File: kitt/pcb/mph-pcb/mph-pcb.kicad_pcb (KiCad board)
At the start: 4 copper layers, 280 x 125 mm, 6 parts

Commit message: prototype layout
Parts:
- added REF**: DF3GD, KITT-Footpads:DF3GD_Light_Bar, F.Cu at (123.8, 80.3)
- added REF**: LED, KITT-Footpads:Flangeless_LED, F.Cu at (122.5, 107.0)
- added REF**: LED, KITT-Footpads:Flangeless_LED, F.Cu at (117.4, 107.0)
- added REF**: LED, KITT-Footpads:Flangeless_LED, F.Cu at (112.3, 107.0)
- added REF**: LED, KITT-Footpads:Flangeless_LED, F.Cu at (107.2, 107.0)
- added REF**: LED, KITT-Footpads:Flangeless_LED, F.Cu at (102.2, 107.0)
- added REF**: LED, KITT-Footpads:Flangeless_LED, F.Cu at (97.1, 107.0)
- added REF**: LED, KITT-Footpads:Flangeless_LED, F.Cu at (92.0, 107.0)
- added REF**: LED, KITT-Footpads:Flangeless_LED, F.Cu at (86.9, 107.0)
- added REF**: LED, KITT-Footpads:Flangeless_LED, F.Cu at (81.8, 107.0)
- added REF**: LED, KITT-Footpads:Flangeless_LED, F.Cu at (76.8, 107.0)
- added REF**: DF3GD, KITT-Footpads:DF3GD_Light_Bar, F.Cu at (103.4, 80.3)
- added REF**: LED, KITT-Footpads:Flangeless_LED, F.Cu at (71.7, 107.0)
- added REF**: LED, KITT-Footpads:Flangeless_LED, F.Cu at (66.6, 107.0)
- added REF**: LED, KITT-Footpads:Flangeless_LED, F.Cu at (61.5, 107.0)
- added REF**: LED, KITT-Footpads:Flangeless_LED, F.Cu at (56.4, 107.0)
- added REF**: LED, KITT-Footpads:Flangeless_LED, F.Cu at (51.4, 107.0)
- added REF**: LED, KITT-Footpads:Flangeless_LED, F.Cu at (48.8, 99.3)
- added REF**: LED, KITT-Footpads:Flangeless_LED, F.Cu at (53.9, 99.3)
- added REF**: LED, KITT-Footpads:Flangeless_LED, F.Cu at (59.0, 99.3)
- added REF**: LED, KITT-Footpads:Flangeless_LED, F.Cu at (117.4, 67.6)
- added REF**: LED, KITT-Footpads:Flangeless_LED, F.Cu at (122.5, 67.6)
- added REF**: DF3GD, KITT-Footpads:DF3GD_Light_Bar, F.Cu at (111.0, 91.7)
- added REF**: LED, KITT-Footpads:Flangeless_LED, F.Cu at (127.6, 67.6)
- added REF**: LED, KITT-Footpads:Flangeless_LED, F.Cu at (165.7, 99.3)
- added REF**: LED, KITT-Footpads:Flangeless_LED, F.Cu at (160.6, 99.3)
- added REF**: LED, KITT-Footpads:Flangeless_LED, F.Cu at (155.5, 99.3)
- added REF**: KB2855SGD, KITT-Footpads:KB2855SGD_Light_Square, F.Cu at (244.4, 84.1)
- added REF**: KB2855SGD, KITT-Footpads:KB2855SGD_Light_Square, F.Cu at (234.2, 84.1)
- added REF**: KB2855SGD, KITT-Footpads:KB2855SGD_Light_Square, F.Cu at (224.1, 84.1)
- added REF**: LDS-A816RI, KITT-Footpads:LDS-A816RI, F.Cu at (196.1, 70.1)
- added REF**: LED, KITT-Footpads:Flangeless_LED, F.Cu at (252.0, 60.0)
- added REF**: LED, KITT-Footpads:Flangeless_LED, F.Cu at (246.9, 60.0)
- added REF**: DF3GD, KITT-Footpads:DF3GD_Light_Bar, F.Cu at (90.7, 91.7)
- added REF**: LED, KITT-Footpads:Flangeless_LED, F.Cu at (241.9, 60.0)
- added REF**: LED, KITT-Footpads:Flangeless_LED, F.Cu at (236.8, 60.0)
- added REF**: LED, KITT-Footpads:Flangeless_LED, F.Cu at (231.7, 60.0)
- added REF**: LED, KITT-Footpads:Flangeless_LED, F.Cu at (226.6, 60.0)
- added REF**: LED, KITT-Footpads:Flangeless_LED, F.Cu at (221.5, 60.0)
- added REF**: LED, KITT-Footpads:Flangeless_LED, F.Cu at (216.5, 60.0)
- added REF**: LED, KITT-Footpads:Flangeless_LED, F.Cu at (211.4, 60.0)
- added REF**: LED, KITT-Footpads:Flangeless_LED, F.Cu at (206.3, 60.0)
- added REF**: LED, KITT-Footpads:Flangeless_LED, F.Cu at (201.2, 60.0)
- added REF**: LED, KITT-Footpads:Flangeless_LED, F.Cu at (196.1, 60.0)
- added REF**: LDS-A816RI, KITT-Footpads:LDS-A816RI, F.Cu at (112.3, 117.1)
- added REF**: LED, KITT-Footpads:Flangeless_LED, F.Cu at (191.1, 60.0)
- added REF**: LED, KITT-Footpads:Flangeless_LED, F.Cu at (186.0, 60.0)
- added REF**: LED, KITT-Footpads:Flangeless_LED, F.Cu at (180.9, 60.0)
- added REF**: LED, KITT-Footpads:Flangeless_LED, F.Cu at (175.8, 60.0)
- added REF**: LED, KITT-Footpads:Flangeless_LED, F.Cu at (170.7, 60.0)
- added REF**: LED, KITT-Footpads:Flangeless_LED, F.Cu at (165.7, 60.0)
- added REF**: LDS-A816RI, KITT-Footpads:LDS-A816RI, F.Cu at (175.8, 70.1)
- added REF**: LDS-A816RI, KITT-Footpads:LDS-A816RI, F.Cu at (155.5, 70.1)
- added REF**: LED, KITT-Footpads:Flangeless_LED, F.Cu at (165.7, 52.3)
- added REF**: LED, KITT-Footpads:Flangeless_LED, F.Cu at (160.6, 52.3)
- added REF**: LDS-A816RI, KITT-Footpads:LDS-A816RI, F.Cu at (92.0, 117.1)
- added REF**: LED, KITT-Footpads:Flangeless_LED, F.Cu at (155.5, 52.3)
- added REF**: LED, KITT-Footpads:Flangeless_LED, F.Cu at (160.6, 59.9)
- added REF**: LED, KITT-Footpads:Flangeless_LED, F.Cu at (155.5, 60.0)
- added REF**: LDS-A816RI, KITT-Footpads:LDS-A816RI, F.Cu at (71.7, 117.1)
- added REF**: LDS-A816RI, KITT-Footpads:LDS-A816RI, F.Cu at (51.4, 117.1)
- added REF**: LED, KITT-Footpads:Flangeless_LED, F.Cu at (127.6, 107.0)
- renumbered UL to MH1, UR to MH2, LR to MH3, LR to MH4
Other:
- board text added: "0"
- board text added: "100"
- board text added: "200"

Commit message: add pegboard holes
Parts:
- added PEG1: MountingHole_6.4mm_M6, MountingHole:MountingHole_6.4mm_M6, F.Cu at (58.1, 77.5)
- added PEG2: MountingHole_6.4mm_M6, MountingHole:MountingHole_6.4mm_M6, F.Cu at (286.7, 52.0)
- added PEG3: MountingHole_6.4mm_M6, MountingHole:MountingHole_6.4mm_M6, F.Cu at (58.1, 153.7)
- added PEG4: MountingHole_6.4mm_M6, MountingHole:MountingHole_6.4mm_M6, F.Cu at (261.3, 153.7)
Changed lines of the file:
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@@
     (tracks 0)
     (zones 0)
-    (modules 68)
+    (modules 72)
     (nets 1)
   )
@@
     (uvia_drill 0.1)
   )
+  (module MountingHole:MountingHole_6.4mm_M6 (layer F.Cu)
+    (at 286.7 52.05)
+    (descr "Mounting Hole 6.4mm, no annular, M6")
+    (tags "mounting hole 6.4mm no annular m6")
+    (attr virtual)
+    (fp_text reference PEG2 (at 0 -7.4) (layer F.SilkS)
+      (effects (font (size 1 1) (thickness 0.15)))
+    )
+    (fp_text value MountingHole_6.4mm_M6 (at 0 7.4) (layer F.Fab)
+      (effects (font (size 1 1) (thickness 0.15)))
+    )
+    (fp_circle (center 0 0) (end 6.65 0) (layer F.CrtYd) (width 0.05))
+    (fp_circle (center 0 0) (end 6.4 0) (layer Cmts.User) (width 0.15))
+    (fp_text user %R (at 0.3 0) (layer F.Fab)
+      (effects (font (size 1 1) (thickness 0.15)))
+    )
+    (pad 1 np_thru_hole circle (at 0 0) (size 6.4 6.4) (drill 6.4) (layers *.Cu *.Mask))
+  )
+  (module MountingHole:MountingHole_6.4mm_M6 (layer F.Cu)
+    (at 261.3 153.65)
+    (descr "Mounting Hole 6.4mm, no annular, M6")
+    (tags "mounting hole 6.4mm no annular m6")
+    (attr virtual)
+    (fp_text reference PEG4 (at 0 -7.4) (layer F.SilkS)
+      (effects (font (size 1 1) (thickness 0.15)))
+    )
+    (fp_text value MountingHole_6.4mm_M6 (at 0 7.4) (layer F.Fab)
+      (effects (font (size 1 1) (thickness 0.15)))
+    )
+    (fp_circle (center 0 0) (end 6.65 0) (layer F.CrtYd) (width 0.05))
+    (fp_circle (center 0 0) (end 6.4 0) (layer Cmts.User) (width 0.15))
+    (fp_text user %R (at 0.3 0) (layer F.Fab)
+      (effects (font (size 1 1) (thickness 0.15)))
+    )
+    (pad 1 np_thru_hole circle (at 0 0) (size 6.4 6.4) (drill 6.4) (layers *.Cu *.Mask))
+  )
+  (module MountingHole:MountingHole_6.4mm_M6 (layer F.Cu)
+    (at 58.1 77.45)
+    (descr "Mounting Hole 6.4mm, no annular, M6")
+    (tags "mounting hole 6.4mm no annular m6")
+    (attr virtual)
+    (fp_text reference PEG1 (at 0 -7.4) (layer F.SilkS)
+      (effects (font (size 1 1) (thickness 0.15)))
+    )
+    (fp_text value MountingHole_6.4mm_M6 (at 0 7.4) (layer F.Fab)
+      (effects (font (size 1 1) (thickness 0.15)))
+    )
+    (fp_circle (center 0 0) (end 6.65 0) (layer F.CrtYd) (width 0.05))
+    (fp_circle (center 0 0) (end 6.4 0) (layer Cmts.User) (width 0.15))
+    (fp_text user %R (at 0.3 0) (layer F.Fab)
+      (effects (font (size 1 1) (thickness 0.15)))
+    )
+    (pad 1 np_thru_hole circle (at 0 0) (size 6.4 6.4) (drill 6.4) (layers *.Cu *.Mask))
+  )
+  (module MountingHole:MountingHole_6.4mm_M6 (layer F.Cu)
+    (at 58.1 153.65)
+    (descr "Mounting Hole 6.4mm, no annular, M6")
+    (tags "mounting hole 6.4mm no annular m6")
+    (attr virtual)
+    (fp_text reference PEG3 (at 0 -7.4) (layer F.SilkS)
+      (effects (font (size 1 1) (thickness 0.15)))
+    )
+    (fp_text value MountingHole_6.4mm_M6 (at 0 7.4) (layer F.Fab)
+      (effects (font (size 1 1) (thickness 0.15)))
+    )
+    (fp_circle (center 0 0) (end 6.65 0) (layer F.CrtYd) (width 0.05))
+    (fp_circle (center 0 0) (end 6.4 0) (layer Cmts.User) (width 0.15))
+    (fp_text user %R (at 0.3 0) (layer F.Fab)
+      (effects (font (size 1 1) (thickness 0.15)))
+    )
+    (pad 1 np_thru_hole circle (at 0 0) (size 6.4 6.4) (drill 6.4) (layers *.Cu *.Mask))
+  )
   (module KITT-Footpads:DF3GD_Light_Bar (layer F.Cu)
     (at 123.75 80.28)
@@
     )
     (fp_text value DF3GD (at -6.4 4.105) (layer F.Fab)
-      (effects (font (size 1 1) (thickness 0.15)))
-    )
-    (fp_text user 6 (at -12.75 2.2) (layer F.SilkS)
-      (effects (font (size 1 1) (thickness 0.15)))
-    )
-    (fp_text user 5 (at -10.21 2.2) (layer F.SilkS)
-      (effects (font (size 1 1) (thickness 0.15)))
-    )
-    (fp_text user 4 (at -7.67 2.2) (layer F.SilkS)
-      (effects (font (size 1 1) (thickness 0.15)))
-    )
-    (fp_text user 3 (at -5.13 2.2) (layer F.SilkS)
-      (effects (font (size 1 1) (thickness 0.15)))
-    )
-    (fp_text user 2 (at -2.59 2.2) (layer F.SilkS)
-      (effects (font (size 1 1) (thickness 0.15)))
-    )
-    (fp_text user 1 (at -0.05 2.2) (layer F.SilkS)
       (effects (font (size 1 1) (thickness 0.15)))
     )
@@
     (fp_line (start 3.55 5.6) (end -16.35 5.6) (layer F.Fab) (width 0.12))
     (fp_line (start -16.35 5.6) (end -16.35 -1.2) (layer F.Fab) (width 0.12))
+    (fp_text user 6 (at -12.75 2.2) (layer F.SilkS)
+      (effects (font (size 1 1) (thickness 0.15)))
+    )
+    (fp_text user 5 (at -10.21 2.2) (layer F.SilkS)
+      (effects (font (size 1 1) (thickness 0.15)))
+    )
+    (fp_text user 4 (at -7.67 2.2) (layer F.SilkS)
+      (effects (font (size 1 1) (thickness 0.15)))
+    )
+    (fp_text user 3 (at -5.13 2.2) (layer F.SilkS)
+      (effects (font (size 1 1) (thickness 0.15)))
+    )
+    (fp_text user 2 (at -2.59 2.2) (layer F.SilkS)
+      (effects (font (size 1 1) (thickness 0.15)))
+    )
+    (fp_text user 1 (at -0.05 2.2) (layer F.SilkS)
+      (effects (font (size 1 1) (thickness 0.15)))
+    )
     (pad 6 thru_hole circle (at -12.75 0) (size 1.524 1.524) (drill 0.762) (layers *.Cu *.Mask))
     (pad 5 thru_hole circle (at -10.21 0) (size 1.524 1.524) (drill 0.762) (layers *.Cu *.Mask))
@@
     )
     (fp_text value DF3GD (at -6.4 4.105) (layer F.Fab)
-      (effects (font (size 1 1) (thickness 0.15)))
-    )
-    (fp_text user 6 (at -12.75 2.2) (layer F.SilkS)
-      (effects (font (size 1 1) (thickness 0.15)))
-    )
-    (fp_text user 5 (at -10.21 2.2) (layer F.SilkS)
-      (effects (font (size 1 1) (thickness 0.15)))
-    )
-    (fp_text user 4 (at -7.67 2.2) (layer F.SilkS)
-      (effects (font (size 1 1) (thickness 0.15)))
-    )
-    (fp_text user 3 (at -5.13 2.2) (layer F.SilkS)
-      (effects (font (size 1 1) (thickness 0.15)))
-    )
-    (fp_text user 2 (at -2.59 2.2) (layer F.SilkS)
-      (effects (font (size 1 1) (thickness 0.15)))
-    )
-    (fp_text user 1 (at -0.05 2.2) (layer F.SilkS)
       (effects (font (size 1 1) (thickness 0.15)))
     )
@@
     (fp_line (start 3.55 5.6) (end -16.35 5.6) (layer F.Fab) (width 0.12))
     (fp_line (start -16.35 5.6) (end -16.35 -1.2) (layer F.Fab) (width 0.12))
+    (fp_text user 6 (at -12.75 2.2) (layer F.SilkS)
+      (effects (font (size 1 1) (thickness 0.15)))
+    )
+    (fp_text user 5 (at -10.21 2.2) (layer F.SilkS)
+      (effects (font (size 1 1) (thickness 0.15)))
+    )
+    (fp_text user 4 (at -7.67 2.2) (layer F.SilkS)
+      (effects (font (size 1 1) (thickness 0.15)))
+    )
+    (fp_text user 3 (at -5.13 2.2) (layer F.SilkS)
+      (effects (font (size 1 1) (thickness 0.15)))
+    )
+    (fp_text user 2 (at -2.59 2.2) (layer F.SilkS)
+      (effects (font (size 1 1) (thickness 0.15)))
+    )
+    (fp_text user 1 (at -0.05 2.2) (layer F.SilkS)
+      (effects (font (size 1 1) (thickness 0.15)))
+    )
     (pad 6 thru_hole circle (at -12.75 0) (size 1.524 1.524) (drill 0.762) (layers *.Cu *.Mask))
     (pad 5 thru_hole circle (at -10.21 0) (size 1.524 1.524) (drill 0.762) (layers *.Cu *.Mask))
@@
       (effects (font (size 1 1) (thickness 0.15)))
     )
-    (fp_text user 6 (at -12.75 2.2) (layer F.SilkS)
-      (effects (font (size 1 1) (thickness 0.15)))
-    )
-    (fp_text user 5 (at -10.21 2.2) (layer F.SilkS)
-      (effects (font (size 1 1) (thickness 0.15)))
-    )
-    (fp_text user 4 (at -7.67 2.2) (layer F.SilkS)
-      (effects (font (size 1 1) (thickness 0.15)))
-    )
-    (fp_text user 3 (at -5.13 2.2) (layer F.SilkS)
-      (effects (font (size 1 1) (thickness 0.15)))
-    )
-    (fp_text user 2 (at -2.59 2.2) (layer F.SilkS)
-      (effects (font (size 1 1) (thickness 0.15)))
-    )
-    (fp_text user 1 (at -0.05 2.2) (layer F.SilkS)
-      (effects (font (size 1 1) (thickness 0.15)))
-    )
     (fp_line (start -16.35 -1.2) (end -16.35 5.6) (layer F.SilkS) (width 0.12))
     (fp_line (start -16.35 -1.2) (end 3.55 -1.2) (layer F.SilkS) (width 0.12))
@@
     (fp_line (start 3.55 5.6) (end -16.35 5.6) (layer F.Fab) (width 0.12))
     (fp_line (start -16.35 5.6) (end -16.35 -1.2) (layer F.Fab) (width 0.12))
+    (fp_text user 6 (at -12.75 2.2) (layer F.SilkS)
+      (effects (font (size 1 1) (thickness 0.15)))
+    )
+    (fp_text user 5 (at -10.21 2.2) (layer F.SilkS)
+      (effects (font (size 1 1) (thickness 0.15)))
+    )
+    (fp_text user 4 (at -7.67 2.2) (layer F.SilkS)
+      (effects (font (size 1 1) (thickness 0.15)))
+    )
+    (fp_text user 3 (at -5.13 2.2) (layer F.SilkS)
+      (effects (font (size 1 1) (thickness 0.15)))
+    )
+    (fp_text user 2 (at -2.59 2.2) (layer F.SilkS)
+      (effects (font (size 1 1) (thickness 0.15)))
+    )
+    (fp_text user 1 (at -0.05 2.2) (layer F.SilkS)
+      (effects (font (size 1 1) (thickness 0.15)))
+    )
     (pad 6 thru_hole circle (at -12.75 0 180) (size 1.524 1.524) (drill 0.762) (layers *.Cu *.Mask))
     (pad 5 thru_hole circle (at -10.21 0 180) (size 1.524 1.524) (drill 0.762) (layers *.Cu *.Mask))

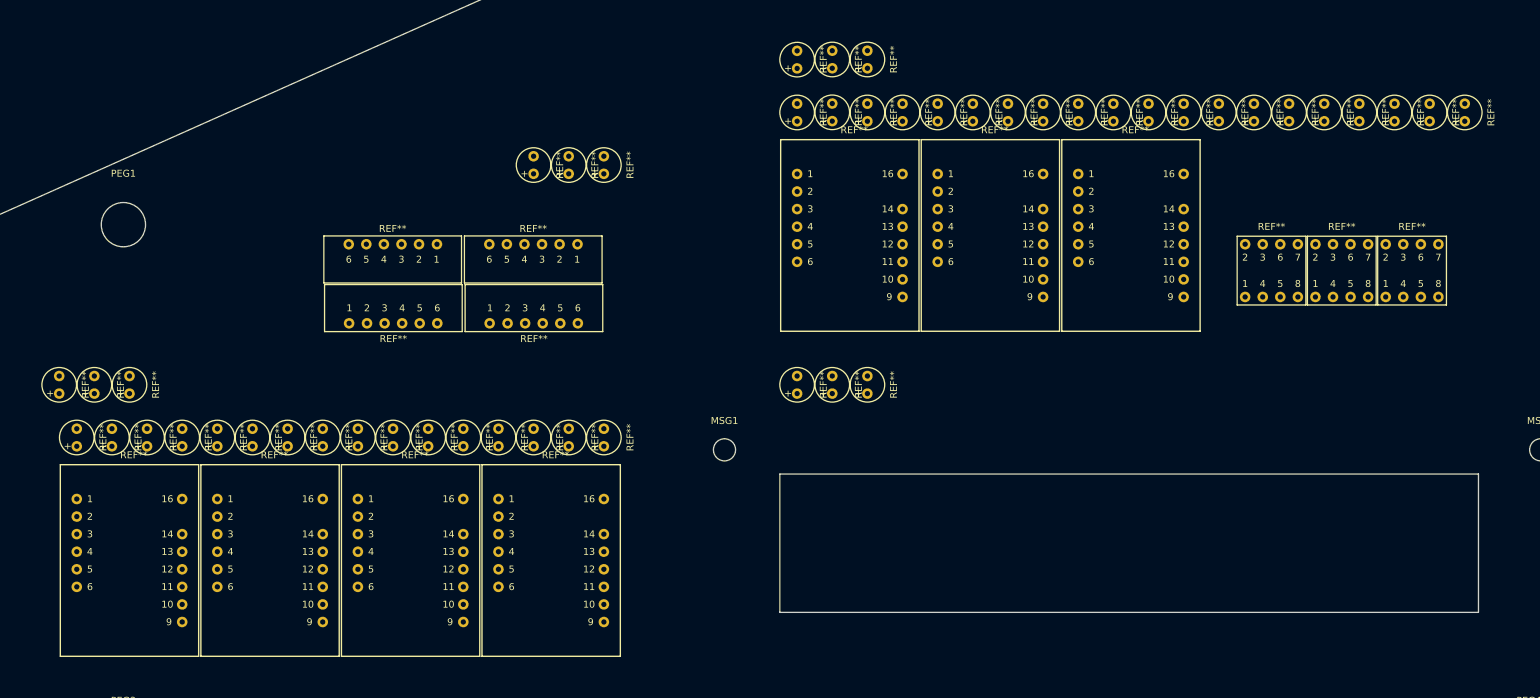
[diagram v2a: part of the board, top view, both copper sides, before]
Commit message: removed dummy components
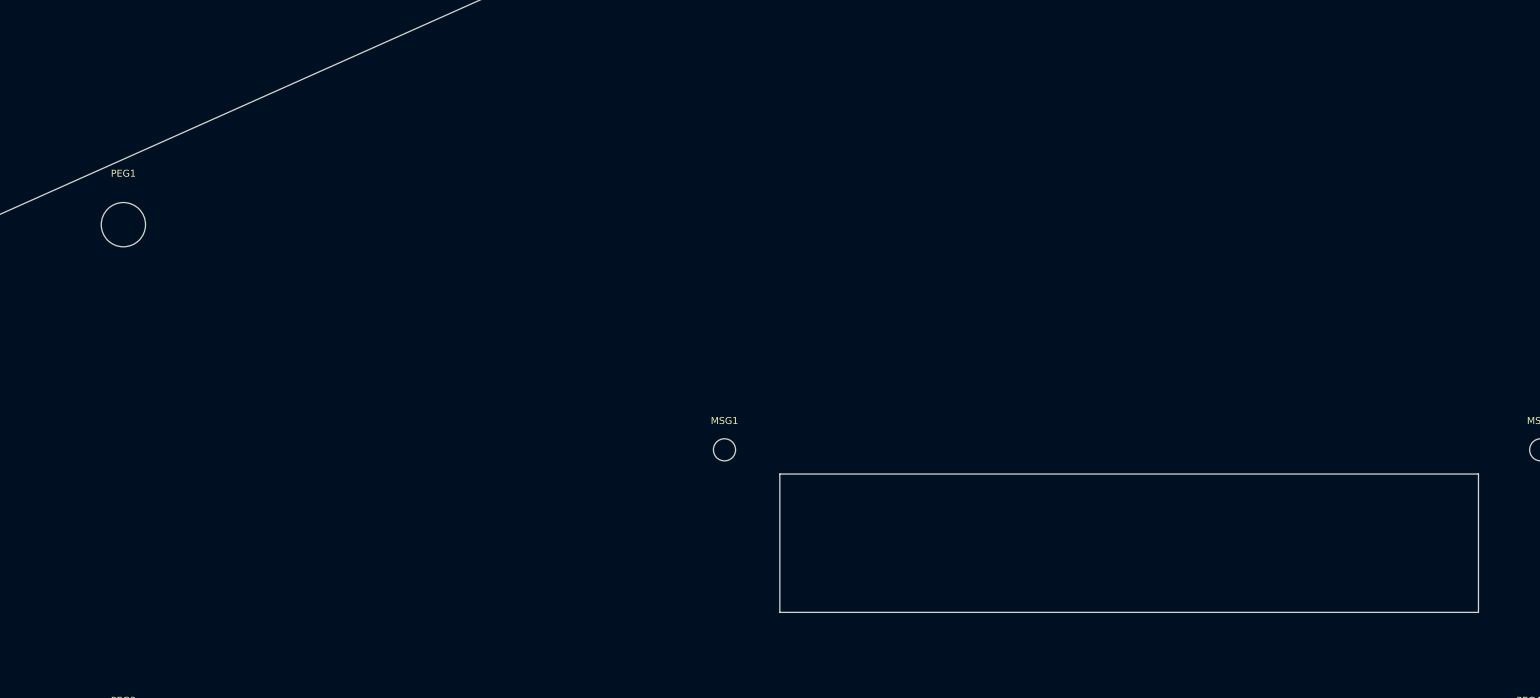
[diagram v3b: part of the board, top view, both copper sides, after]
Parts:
- removed REF** (x4): DF3GD, KITT-Footpads:DF3GD_Light_Bar
- removed REF** (x48): LED, KITT-Footpads:Flangeless_LED
- removed REF** (x3): KB2855SGD, KITT-Footpads:KB2855SGD_Light_Square
- removed REF** (x7): LDS-A816RI, KITT-Footpads:LDS-A816RI
